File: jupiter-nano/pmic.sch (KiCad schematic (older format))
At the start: 52 parts, among them Q1 BSS138, Q2 BSS138, Q3 BSS138, Q4 BSS138, Q5 BSS138, SW1 SW_Push, SW2 SW_Push, U2 ACT8945AQJ305-T

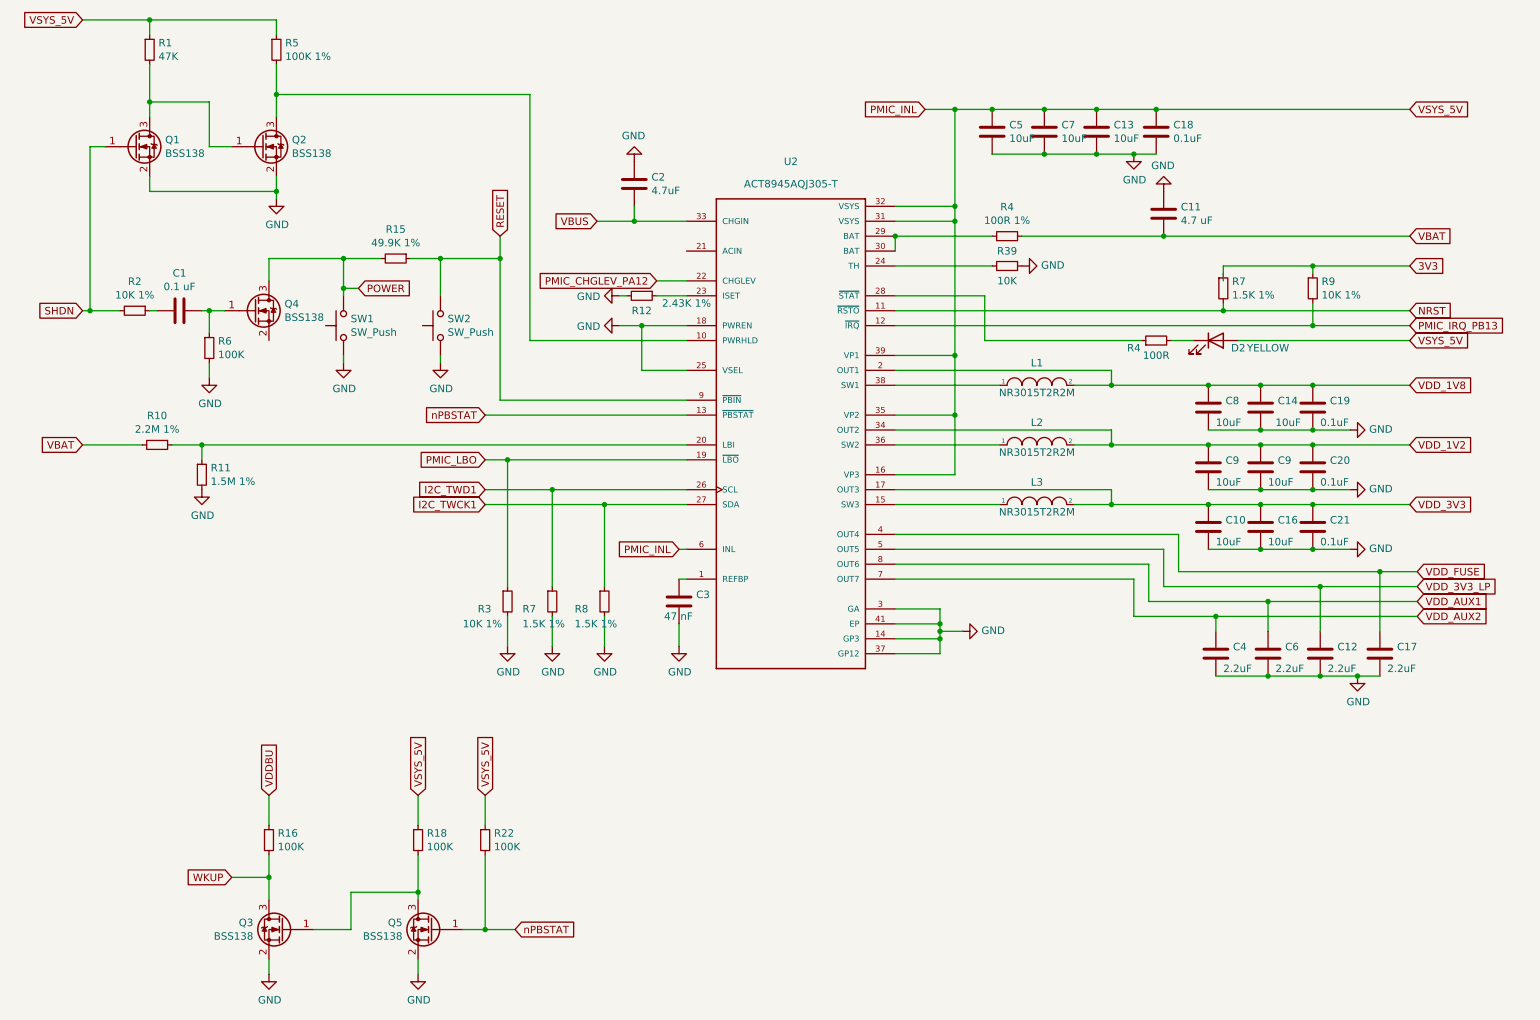
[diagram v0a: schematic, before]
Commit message: numerous ERC fixes
- still more to go
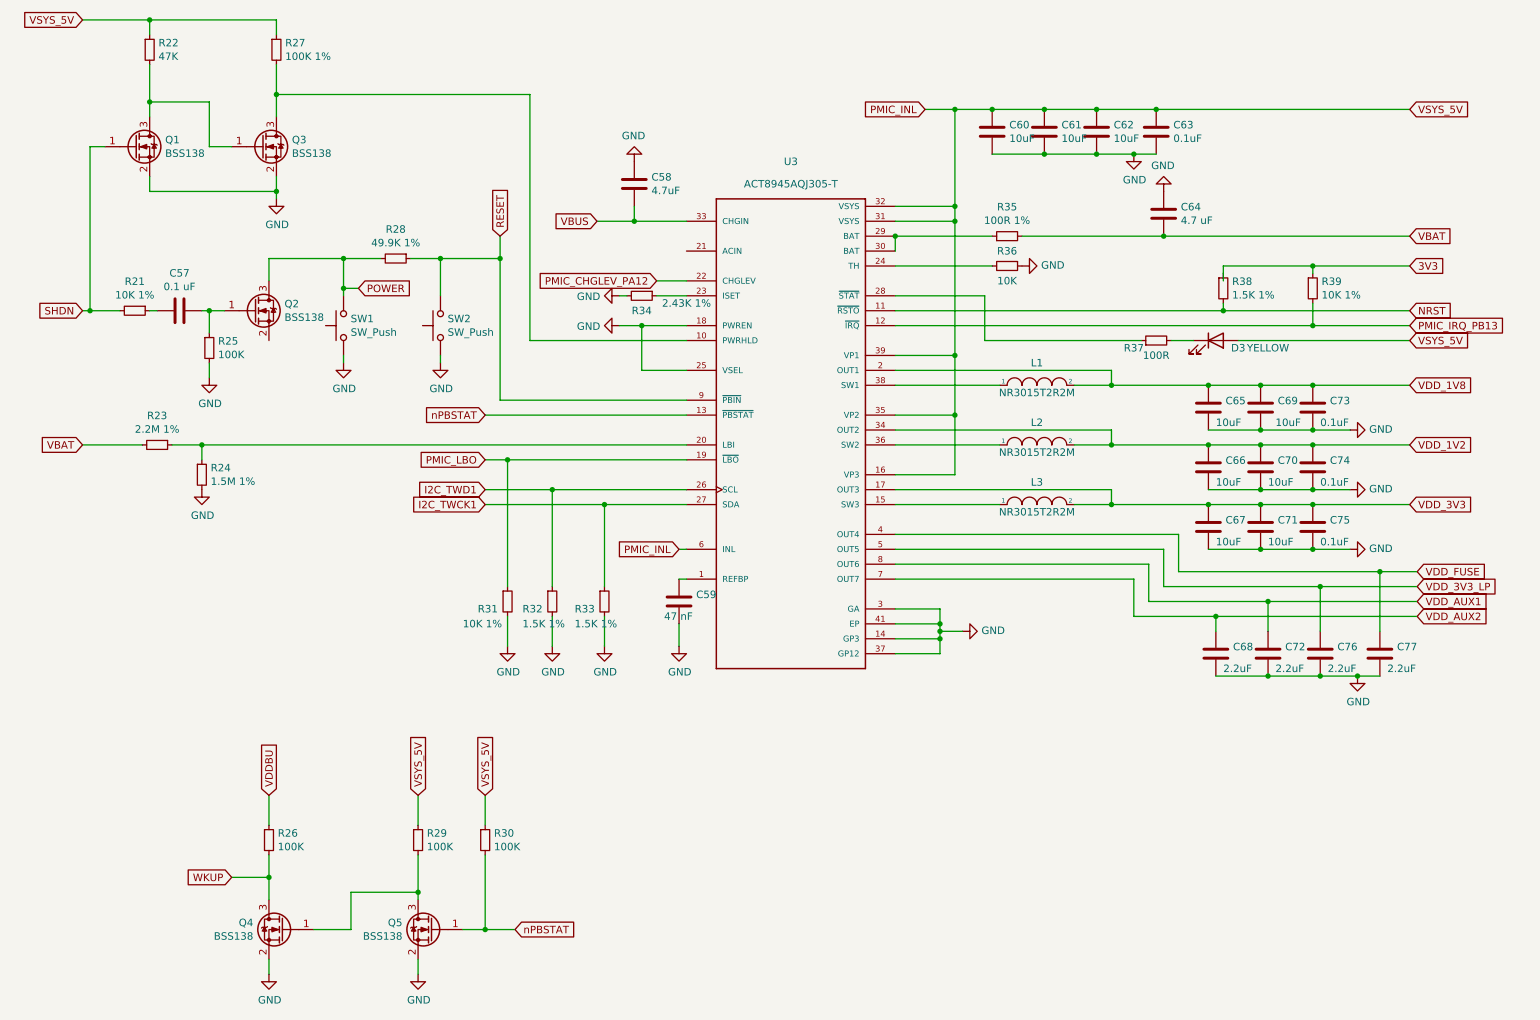
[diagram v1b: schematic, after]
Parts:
- renumbered C1 to C57, C2 to C58, C3 to C59, C5 to C60, C7 to C61, C13 to C62, C18 to C63, C11 to C64, C8 to C65, C9 to C66, C10 to C67, C4 to C68, C14 to C69, C9 to C70, C16 to C71, C6 to C72, C19 to C73, C20 to C74, C21 to C75, C12 to C76, C17 to C77, D2 to D3, Q4 to Q2, Q2 to Q3, Q3 to Q4, R2 to R21, R1 to R22, R10 to R23, R11 to R24, R6 to R25, R16 to R26, R5 to R27, R15 to R28, R18 to R29, R22 to R30, R3 to R31, R7 to R32, R8 to R33, R12 to R34, R4 to R35, R39 to R36, R4 to R37, R7 to R38, R9 to R39, U2 to U3

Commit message: added at24csw080 I2C EEPROM UUID chip
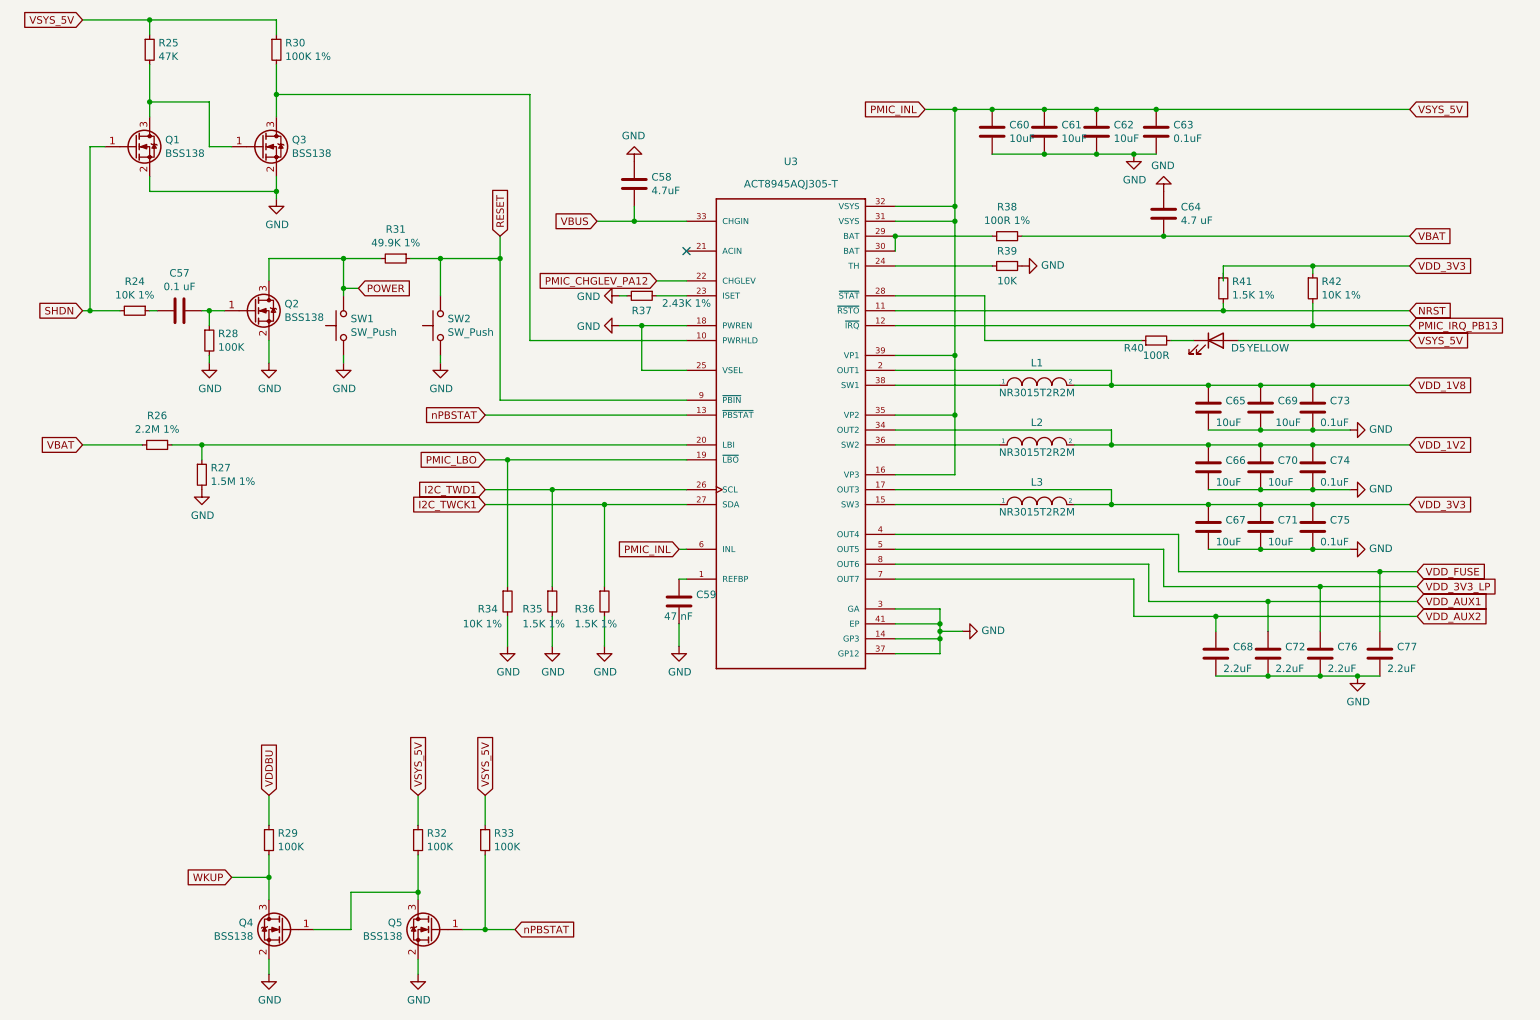
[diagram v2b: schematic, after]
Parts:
- renumbered D3 to D5, R21 to R24, R22 to R25, R23 to R26, R24 to R27, R25 to R28, R26 to R29, R27 to R30, R28 to R31, R29 to R32, R30 to R33, R31 to R34, R32 to R35, R33 to R36, R34 to R37, R35 to R38, R36 to R39, R37 to R40, R38 to R41, R39 to R42
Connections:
- net 3V3 is gone; now on net VDD_3V3: R41.1, R42.1
- net GND: now also Q2.2 (S)
- no-connect marks 0 -> 1
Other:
- moved on the sheet: R28
